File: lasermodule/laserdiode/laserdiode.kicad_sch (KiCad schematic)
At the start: 15 parts, among them J1 Conn_01x04, J2 Conn_01x01, J3 Conn_01x01, J4 Conn_01x01, J5 Conn_01x01, J6 Conn_01x01, J7 Conn_01x01

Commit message: added kicost tracking other plates, fixed plates
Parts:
- J2, J3, J4: manuf# (none) -> 0906-1-15-20-75-14-11-0; mouser# (none) -> 575-906115
- J5: Mouser 575-906115 -> (none); Producer 0906-1-15-20-75-14-11-0 -> (none); manuf# (none) -> 0906-1-15-20-75-14-11-0; mouser# (none) -> 575-906115
- J6: manuf# (none) -> 74663125R; mouser# (none) -> 710-74663125R
- J7: Mouser 575-906115 -> (none); Producer 0906-1-15-20-75-14-11-0 -> (none); manuf# (none) -> 74663125R; mouser# (none) -> 710-74663125R
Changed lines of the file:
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@@
+			)
+		)
+		(property "manuf#" "74663125R"
+			(at 157.48 59.69 0)
+			(effects
+				(font
+					(size 1.27 1.27)
+				)
+				(hide yes)
+			)
+		)
+		(property "mouser#" "710-74663125R"
+			(at 157.48 59.69 0)
+			(effects
+				(font
+					(size 1.27 1.27)
+				)
+				(hide yes)
 			)
 		)
@@
 			)
 		)
+		(property "manuf#" "0906-1-15-20-75-14-11-0"
+			(at 133.35 55.88 0)
+			(effects
+				(font
+					(size 1.27 1.27)
+				)
+				(hide yes)
+			)
+		)
+		(property "mouser#" "575-906115"
+			(at 133.35 55.88 0)
+			(effects
+				(font
+					(size 1.27 1.27)
+				)
+				(hide yes)
+			)
+		)
 		(pin "1"
 		)
@@
 			)
 		)
-		(property "Producer" "0906-1-15-20-75-14-11-0"
+		(property "manuf#" "0906-1-15-20-75-14-11-0"
 			(at 133.35 50.8 0)
 			(effects
@@
 			)
 		)
-		(property "Mouser" "575-906115"
+		(property "mouser#" "575-906115"
 			(at 133.35 50.8 0)
 			(effects
@@
 			)
 		)
-		(property "Producer" "0906-1-15-20-75-14-11-0"
+		(property "manuf#" "74663125R"
 			(at 157.48 50.8 0)
 			(effects
@@
 			)
 		)
-		(property "Mouser" "575-906115"
+		(property "mouser#" "710-74663125R"
 			(at 157.48 50.8 0)
 			(effects
@@
 			)
 		)
+		(property "manuf#" "0906-1-15-20-75-14-11-0"
+			(at 133.35 60.96 0)
+			(effects
+				(font
+					(size 1.27 1.27)
+				)
+				(hide yes)
+			)
+		)
+		(property "mouser#" "575-906115"
+			(at 133.35 60.96 0)
+			(effects
+				(font
+					(size 1.27 1.27)
+				)
+				(hide yes)
+			)
+		)
 		(pin "1"
 		)
@@
 			(at 133.35 66.04 0)
 			(effects
+				(font
+					(size 1.27 1.27)
+				)
+				(hide yes)
+			)
+		)
+		(property "manuf#" "0906-1-15-20-75-14-11-0"
+			(at 133.35 66.04 0)
+			(effects
+				(font
+					(size 1.27 1.27)
+				)
+				(hide yes)
+			)
+		)
+		(property "mouser#" "575-906115"
+			(at 133.35 66.04 0)
+			(effects

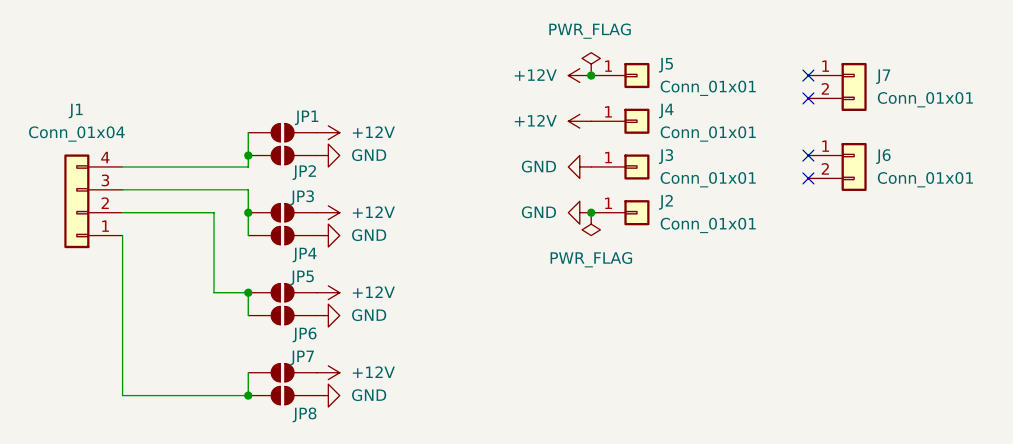
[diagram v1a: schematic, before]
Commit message: fixed typo, added standoff lasermodule
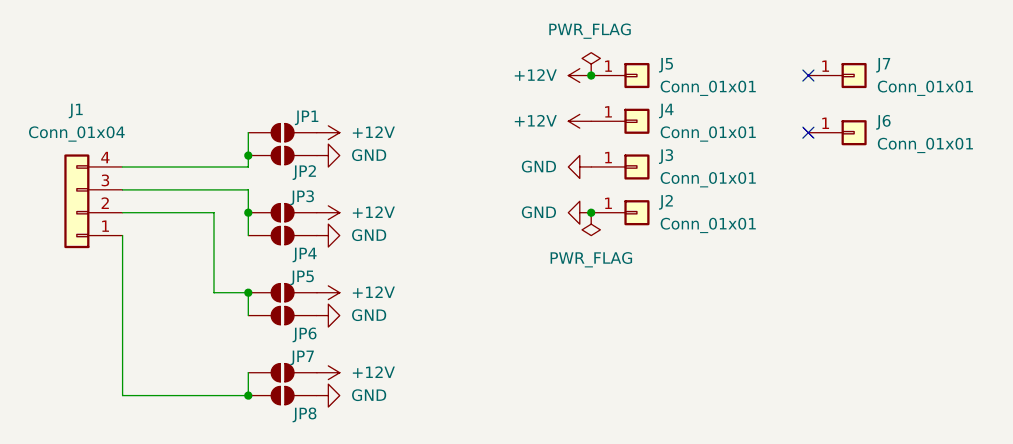
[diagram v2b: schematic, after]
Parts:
- J6, J7: symbol Connector_Generic:Conn_01x02 -> Connector_Generic:Conn_01x01
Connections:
- no-connect marks 4 -> 2
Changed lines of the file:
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@@
 	)
 	(no_connect
-		(at 152.4 62.23)
-	)
-	(no_connect
-		(at 152.4 59.69)
-	)
-	(no_connect
-		(at 152.4 53.34)
+		(at 152.4 57.15)
 	)
 	(wire
@@
 	)
 	(symbol
-		(lib_id "Connector_Generic:Conn_01x02")
-		(at 157.48 59.69 0)
+		(lib_id "Connector_Generic:Conn_01x01")
+		(at 157.48 57.15 0)
 		(unit 1)
 		(exclude_from_sim no)
@@
 		(fields_autoplaced yes)
 		(property "Reference" "J6"
-			(at 160.02 59.6899 0)
+			(at 160.02 55.8799 0)
 			(effects
 				(font
@@
 		)
 		(property "Value" "Conn_01x01"
-			(at 160.02 62.2299 0)
+			(at 160.02 58.4199 0)
 			(effects
 				(font
@@
 		)
 		(property "Footprint" "laserdiode:23765912"
-			(at 157.48 59.69 0)
+			(at 157.48 57.15 0)
 			(effects
 				(font
@@
 		)
 		(property "Datasheet" "~"
-			(at 157.48 59.69 0)
-			(effects
-				(font
-					(size 1.27 1.27)
-				)
-				(hide yes)
-			)
-		)
-		(property "Description" "Generic connector, single row, 01x02, script generated (kicad-library-utils/schlib/autogen/connector/)"
-			(at 157.48 59.69 0)
+			(at 157.48 57.15 0)
+			(effects
+				(font
+					(size 1.27 1.27)
+				)
+				(hide yes)
+			)
+		)
+		(property "Description" "Generic connector, single row, 01x01, script generated (kicad-library-utils/schlib/autogen/connector/)"
+			(at 157.48 57.15 0)
 			(effects
 				(font
@@
 		)
 		(property "Producer" "0906-1-15-20-75-14-11-0"
-			(at 157.48 59.69 0)
+			(at 157.48 57.15 0)
 			(effects
 				(font
@@
 		)
 		(property "Mouser" "575-906115"
-			(at 157.48 59.69 0)
+			(at 157.48 57.15 0)
 			(effects
 				(font
@@
 		)
 		(property "manuf#" "74663125R"
-			(at 157.48 59.69 0)
+			(at 157.48 57.15 0)
 			(effects
 				(font
@@
 		)
 		(property "mouser#" "710-74663125R"
-			(at 157.48 59.69 0)
-			(effects
-				(font
-					(size 1.27 1.27)
-				)
-				(hide yes)
-			)
-		)
-		(pin "1"
-		)
-		(pin "2"
+			(at 157.48 57.15 0)
+			(effects
+				(font
+					(size 1.27 1.27)
+				)
+				(hide yes)
+			)
+		)
+		(pin "1"
 		)
 		(instances
@@
 	)
 	(symbol
-		(lib_id "Connector_Generic:Conn_01x02")
+		(lib_id "Connector_Generic:Conn_01x01")
 		(at 157.48 50.8 0)
 		(unit 1)
@@
 		(fields_autoplaced yes)
 		(property "Reference" "J7"
-			(at 160.02 50.7999 0)
+			(at 160.02 49.5299 0)
 			(effects
 				(font
@@
 		)
 		(property "Value" "Conn_01x01"
-			(at 160.02 53.3399 0)
+			(at 160.02 52.0699 0)
 			(effects
 				(font
@@
 			)
 		)
-		(property "Description" "Generic connector, single row, 01x02, script generated (kicad-library-utils/schlib/autogen/connector/)"
+		(property "Description" "Generic connector, single row, 01x01, script generated (kicad-library-utils/schlib/autogen/connector/)"
 			(at 157.48 50.8 0)
 			(effects
@@
 		(pin "1"
 		)
-		(pin "2"
-		)
-		(instances
+		(instances
